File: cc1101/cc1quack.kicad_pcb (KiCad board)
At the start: 4 copper layers, 59 x 39 mm, 72 parts, among them J103 Conn_01x06_Pin, J201 USB_C_Receptacle, J401 Conn_ARM_JTAG_SWD_10, J402 Conn_01x02, J501 Conn_Coaxial, SW401 Alps SKRTLAE010, U301 XC6206P332MR, U401 STM32F401RCT6, U501 Ebyte-E07-900MM10S, Y401 8MHz 20pF

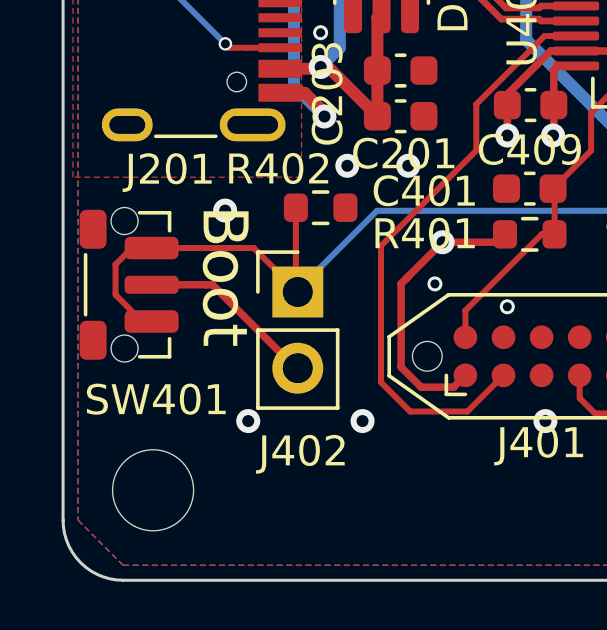
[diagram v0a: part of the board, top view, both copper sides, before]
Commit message: cc1quack: Add specialized switch footprint
Specialize the ALPS SKRTLAE010 to include project-specific 3D model
paths.

Signed-off-by: Andreas Sandberg <andreas@sandberg.uk>
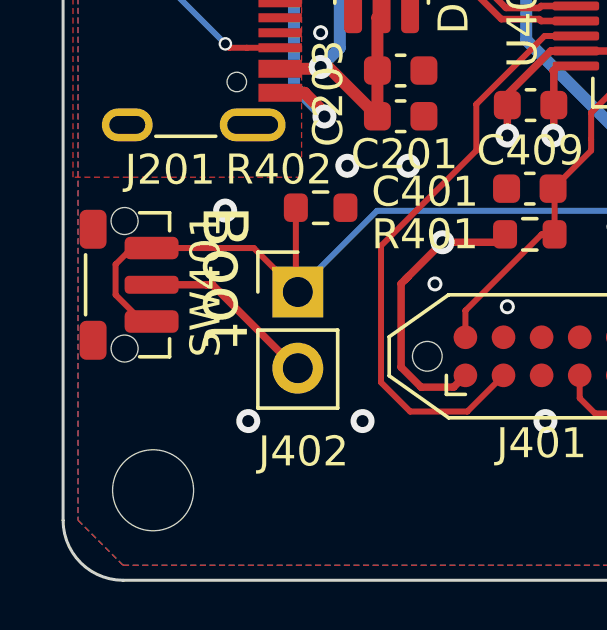
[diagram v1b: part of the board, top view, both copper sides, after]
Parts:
- SW401: footprint Button_Switch_SMD:SW_Push_1P1T-MP_NO_Horizontal_Alps_SKRTLAE010 -> quack:SW_Push_1P1T-MP_NO_Horizontal_Alps_SKRTLAE010
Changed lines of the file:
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@@
     )
   )
-  (footprint "Button_Switch_SMD:SW_Push_1P1T-MP_NO_Horizontal_Alps_SKRTLAE010" (layer "F.Cu")
+  (footprint "quack:SW_Push_1P1T-MP_NO_Horizontal_Alps_SKRTLAE010" (layer "F.Cu")
     (at 102.05 79.15 -90)
     (descr "Side push button (https://www.alps.com/prod/info/E/PDF/Tact/SurfaceMount/SKRT/SKRT.pdf)")
@@
     (property "ki_keywords" "switch lever")
     (attr smd)
-    (fp_text reference "SW401" (at 3.85 -1.074) (layer "F.SilkS")
+    (fp_text reference "SW401" (at 0 -2.7 90) (layer "F.SilkS")
         (effects (font (size 1 1) (thickness 0.15)))
     )
-    (fp_text value "Alps SKRTLAE010" (at 0 2.9 90) (layer "F.Fab")
+    (fp_text value "Alps SKRTLAE010" (at 0 2.9 -90) (layer "F.Fab")
         (effects (font (size 1 1) (thickness 0.15)))
     )
-    (fp_text user "${REFERENCE}" (at 0 0 90) (layer "F.Fab")
+    (fp_text user "${REFERENCE}" (at 0 0 -90) (layer "F.Fab")
         (effects (font (size 1 1) (thickness 0.15)))
     )
@@
       (rotate (xyz 0 0 0))
     )
+    (model "${KIPRJMOD}/3dmodels/SW_Push_1P1T-MP_NO_Horizontal_Alps_SKRTLAE010.stp"
+      (offset (xyz 0 0 0))
+      (scale (xyz 1 1 1))
+      (rotate (xyz -90 0 0))
+    )
+    (model "${KIPRJMOD}/3dmodels/SW_Push_1P1T-MP_NO_Horizontal_Alps_SKRTLAE010.wrl"
+      (offset (xyz 0 0 0))
+      (scale (xyz 1 1 1))
+      (rotate (xyz -90 0 0))
+    )
   )
